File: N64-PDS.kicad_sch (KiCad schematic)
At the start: 39 parts, among them J2 USB-C-6P-PWR, J3 PWR_OUT, J4 I2C_OUT, U1 ST1S41PHR, U2 ST1S41PHR, U3 STUSB4500QTR, U4 STL6P3LLH6

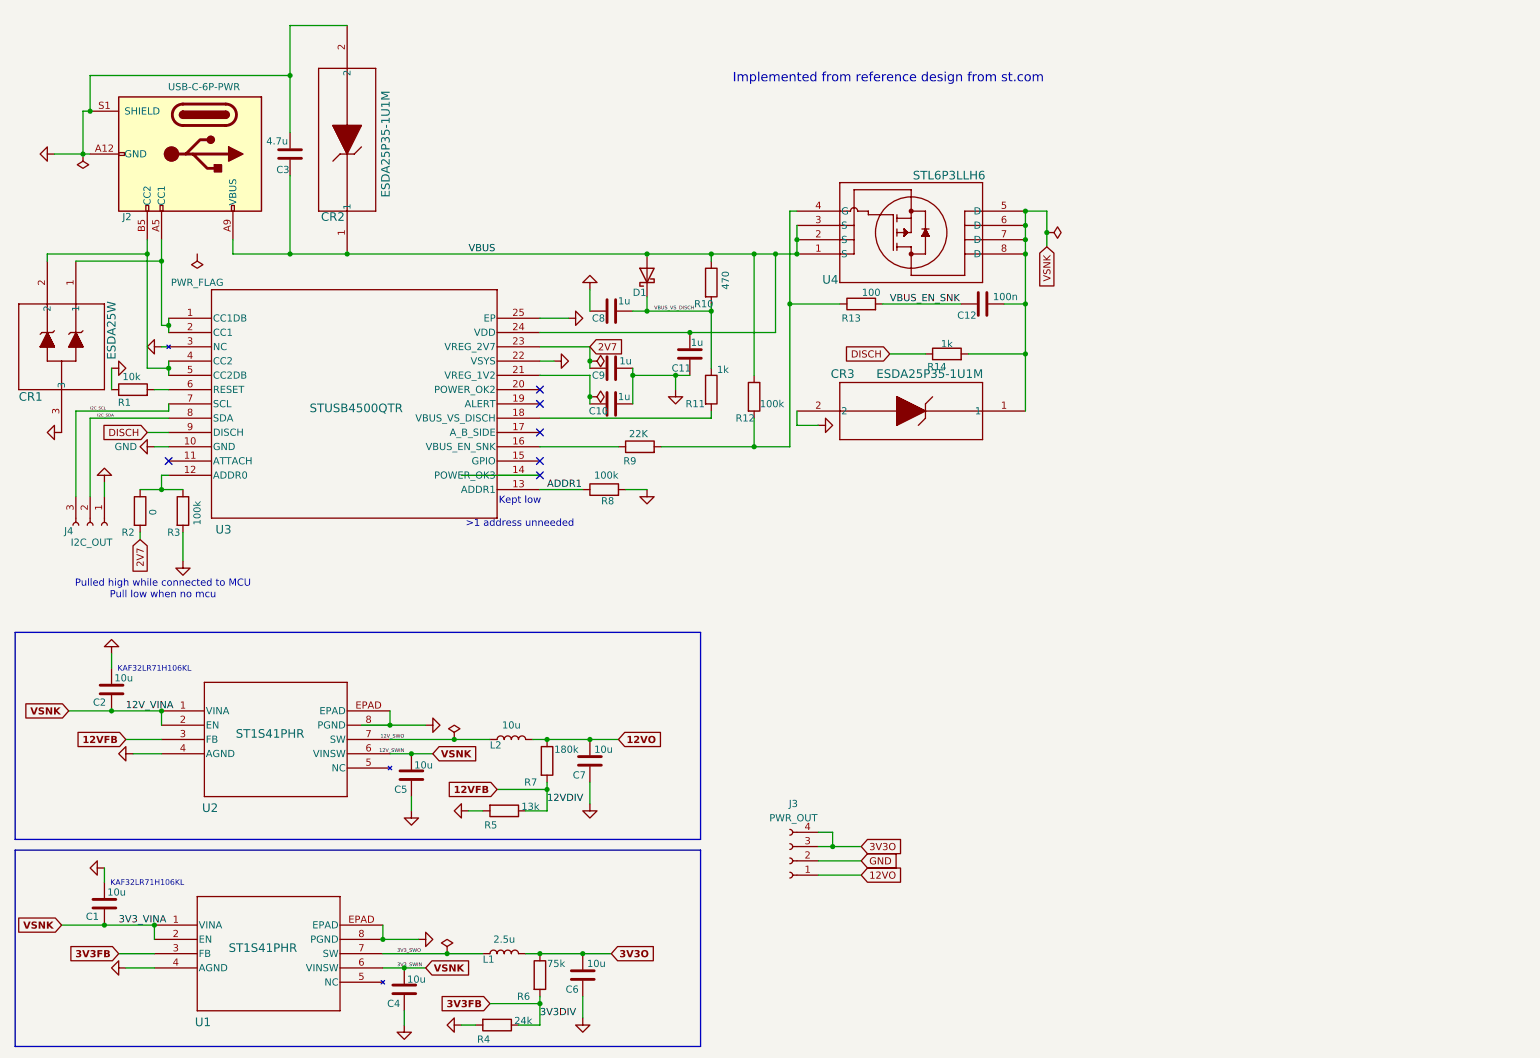
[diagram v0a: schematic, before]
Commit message: Update annotations
Whoopsy!!
I updated all the annotations geographically on the pcb and didnt update the schematic from the pcb, all fixed :)
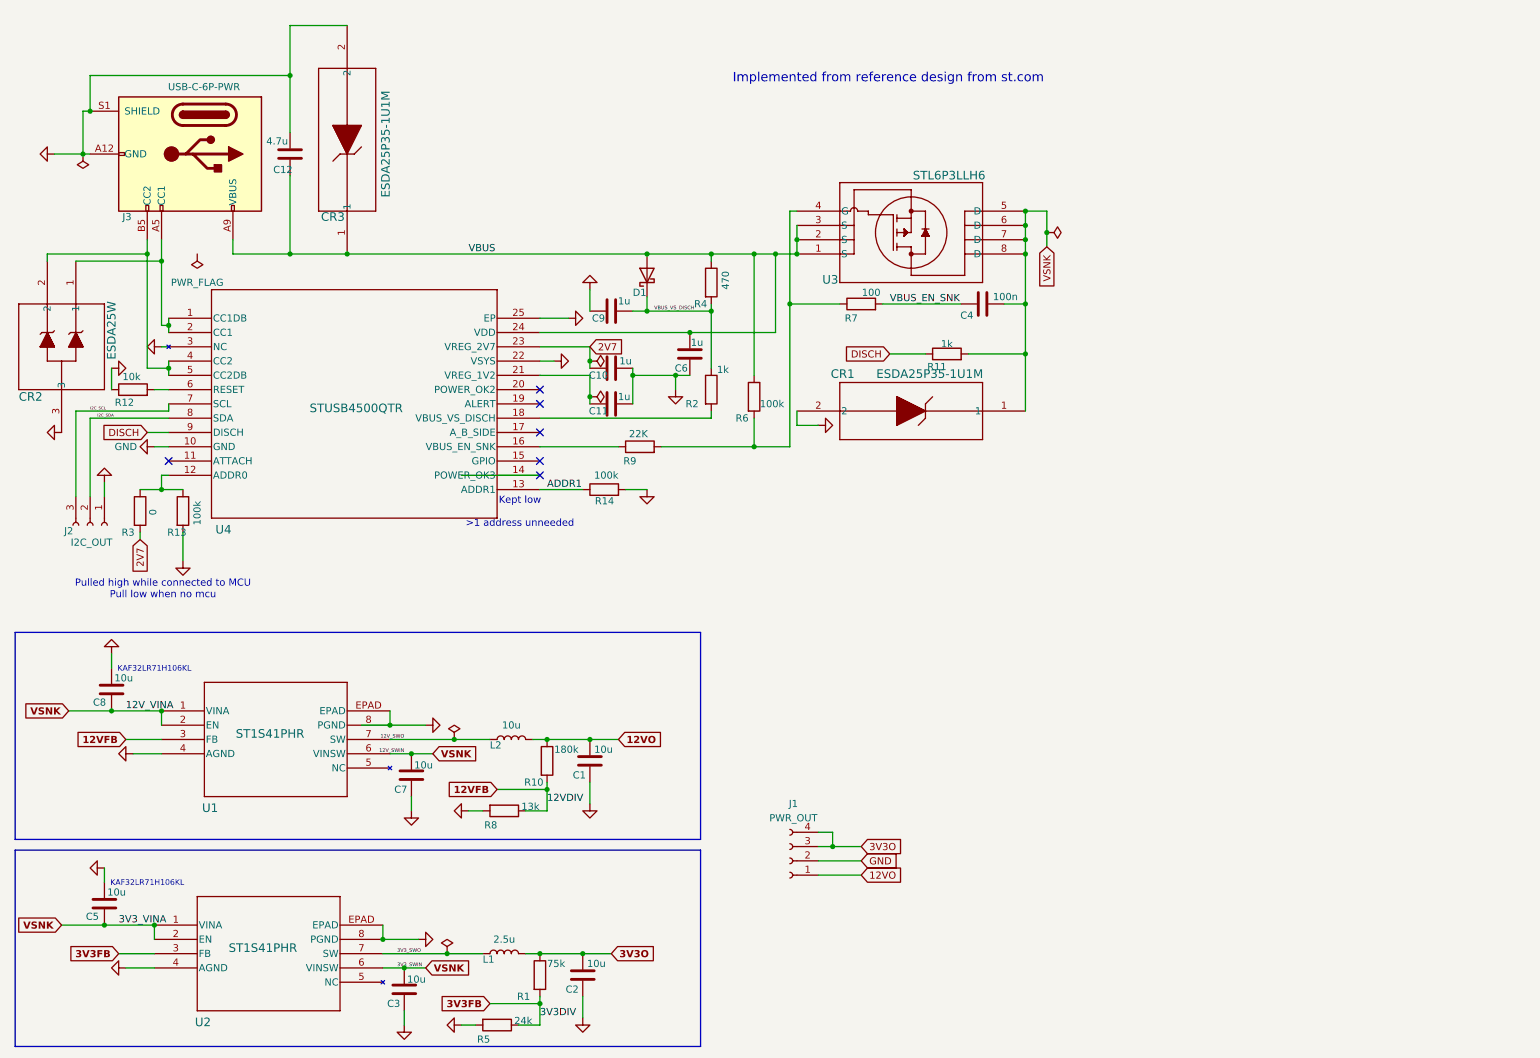
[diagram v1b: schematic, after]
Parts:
- renumbered C7 to C1, C9 to C10, C10 to C11, C3 to C12, C6 to C2, C4 to C3, C12 to C4, C1 to C5, C11 to C6, C5 to C7, C2 to C8, C8 to C9, CR3 to CR1, CR1 to CR2, CR2 to CR3, J3 to J1, J4 to J2, J2 to J3, R6 to R1, R7 to R10, R14 to R11, R1 to R12, R3 to R13, R8 to R14, R11 to R2, R2 to R3, R10 to R4, R4 to R5, R12 to R6, R13 to R7, R5 to R8, U2 to U1, U1 to U2, U4 to U3, U3 to U4

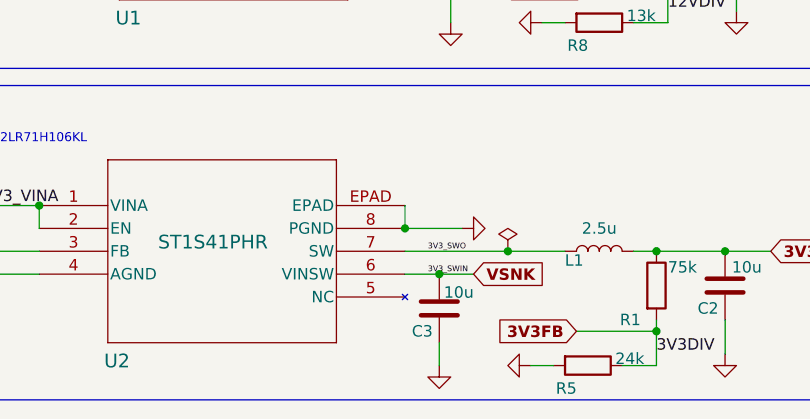
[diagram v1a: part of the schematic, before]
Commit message: Update PCB
slight reshuffle of the PCB in the aim of reducing noise from smps
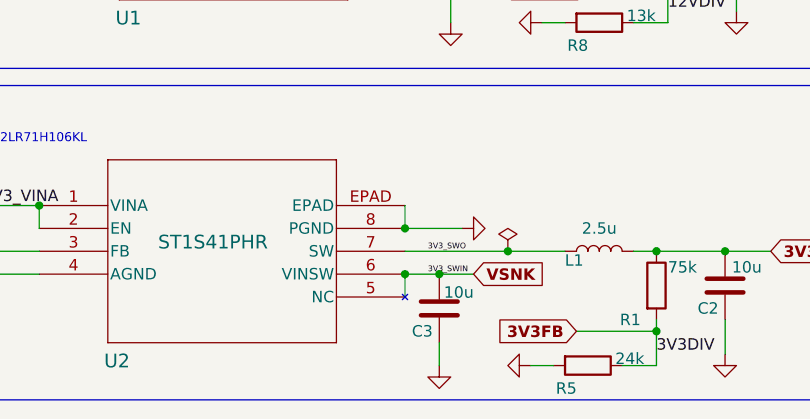
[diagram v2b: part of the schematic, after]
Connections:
- net VSNK: now also U2.5 (NC)
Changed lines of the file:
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@@
+	)
+	(junction
+		(at 80.01 182.88)
+		(diameter 0)
+		(color 0 0 0 0)
 	)
 	(junction
@@
 		)
 		(stroke
+			(width 0)
+			(type default)
+		)
+	)
+	(wire
+		(pts
+			(xy 80.01 182.88) (xy 80.01 185.42)
+		)
+		(stroke

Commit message: Re-route
Re-route to improve design, further updates to come
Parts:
- removed CR1: ESDA25P35-1U1M, ESDA25P35:QFN1610_STM-M, symbol ESDA25P35:ESDA25P35-1U1M
- C12: footprint Capacitor_SMD:C_0402_1005Metric_Pad0.74x0.62mm_HandSolder -> Capacitor_SMD:C_0805_2012Metric_Pad1.18x1.45mm_HandSolder
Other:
- moved on the sheet: R11
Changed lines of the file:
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@@
 	)
 	(junction
-		(at 194.31 73.66)
-		(diameter 0)
-		(color 0 0 0 0)
-	)
-	(junction
 		(at 160.02 161.29)
 		(diameter 0)
@@
 	(wire
 		(pts
-			(xy 153.67 86.36) (xy 157.48 86.36)
-		)
-		(stroke
-			(width 0)
-			(type default)
-		)
-	)
-	(wire
-		(pts
 			(xy 26.67 38.1) (xy 27.94 38.1)
 		)
@@
 	(wire
 		(pts
-			(xy 153.67 83.82) (xy 153.67 86.36)
-		)
-		(stroke
-			(width 0)
-			(type default)
-		)
-	)
-	(wire
-		(pts
 			(xy 91.44 180.34) (xy 97.79 180.34)
 		)
@@
 	(wire
 		(pts
+			(xy 170.18 69.85) (xy 176.53 69.85)
+		)
+		(stroke
+			(width 0)
+			(type default)
+		)
+	)
+	(wire
+		(pts
 			(xy 127 97.79) (xy 123.19 97.79)
 		)
@@
 	(wire
 		(pts
-			(xy 184.15 73.66) (xy 194.31 73.66)
+			(xy 184.15 69.85) (xy 194.31 69.85)
 		)
 		(stroke
@@
 	(wire
 		(pts
-			(xy 194.31 64.77) (xy 194.31 73.66)
+			(xy 194.31 64.77) (xy 194.31 69.85)
 		)
 		(stroke
@@
 	(wire
 		(pts
-			(xy 170.18 73.66) (xy 176.53 73.66)
-		)
-		(stroke
-			(width 0)
-			(type default)
-		)
-	)
-	(wire
-		(pts
 			(xy 153.67 50.8) (xy 153.67 53.34)
 		)
@@
 		)
 	)
-	(wire
-		(pts
-			(xy 194.31 73.66) (xy 194.31 83.82)
-		)
-		(stroke
-			(width 0)
-			(type default)
-		)
-	)
 	(rectangle
 		(start 14.605 123.19)
@@
 	(global_label "DISCH"
 		(shape input)
-		(at 170.18 73.66 180)
+		(at 170.18 69.85 180)
 		(fields_autoplaced yes)
 		(effects
@@
 		)
 		(property "Intersheetrefs" "${INTERSHEET_REFS}"
-			(at 161.51 73.66 0)
+			(at 161.51 69.85 0)
 			(effects
 				(font
@@
 			)
 		)
-		(property "Footprint" "Capacitor_SMD:C_0402_1005Metric_Pad0.74x0.62mm_HandSolder"
+		(property "Footprint" "Capacitor_SMD:C_0805_2012Metric_Pad1.18x1.45mm_HandSolder"
 			(at 62.5348 34.29 0)
 			(effects
@@
 	)
 	(symbol
-		(lib_id "power:GND")
-		(at 157.48 86.36 90)
-		(unit 1)
-		(exclude_from_sim no)
-		(in_bom yes)
-		(on_board yes)
-		(dnp no)
-		(property "Reference" "#PWR05"
-			(at 163.83 86.36 0)
-			(effects
-				(font
-					(size 1.27 1.27)
-				)
-				(hide yes)
-			)
-		)
-		(property "Value" "GND"
-			(at 162.56 86.36 90)
-			(effects
-				(font
-					(size 1.27 1.27)
-				)
-				(hide yes)
-			)
-		)
-		(property "Footprint" ""
-			(at 157.48 86.36 0)
-			(effects
-				(font
-					(size 1.27 1.27)
-				)
-				(hide yes)
-			)
-		)
-		(property "Datasheet" ""
-			(at 157.48 86.36 0)
-			(effects
-				(font
-					(size 1.27 1.27)
-				)
-				(hide yes)
-			)
-		)
-		(property "Description" "Power symbol creates a global label with name \"GND\" , ground"
-			(at 157.48 86.36 0)
-			(effects
-				(font
-					(size 1.27 1.27)
-				)
-				(hide yes)
-			)
-		)
-		(pin "1"
-		)
-		(instances
-			(project "N64-PDS"
-				(path "/9649f91c-0b3c-463e-88a6-37fb387993ef"
-					(reference "#PWR05")
-					(unit 1)
-				)
-			)
-		)
-	)
-	(symbol
 		(lib_id "Device:R")
 		(at 35.56 80.01 90)
@@
 	)
 	(symbol
-		(lib_id "ESDA25P35:ESDA25P35-1U1M")
-		(at 194.31 83.82 0)
-		(mirror y)
-		(unit 1)
-		(exclude_from_sim no)
-		(in_bom yes)
-		(on_board yes)
-		(dnp no)
-		(property "Reference" "CR1"
-			(at 161.798 77.216 0)
-			(effects
-				(font
-					(size 1.524 1.524)
-				)
-			)
-		)
-		(property "Value" "ESDA25P35-1U1M"
-			(at 177.292 77.216 0)
-			(effects
-				(font
-					(size 1.524 1.524)
-				)
-			)
-		)
-		(property "Footprint" "ESDA25P35:QFN1610_STM-M"
-			(at 194.31 83.82 0)
-			(effects
-				(font
-					(size 1.27 1.27)
-					(italic yes)
-				)
-				(hide yes)
-			)
-		)
-		(property "Datasheet" "ESDA25P35-1U1M"
-			(at 194.31 83.82 0)
-			(effects
-				(font
-					(size 1.27 1.27)
-					(italic yes)
-				)
-				(hide yes)
-			)
-		)
-		(property "Description" ""
-			(at 194.31 83.82 0)
-			(effects
-				(font
-					(size 1.27 1.27)
-				)
-				(hide yes)
-			)
-		)
-		(pin "1"
-		)
-		(pin "2"
-		)
-		(instances
-			(project ""
-				(path "/9649f91c-0b3c-463e-88a6-37fb387993ef"
-					(reference "CR1")
-					(unit 1)
-				)
-			)
-		)
-	)
-	(symbol
 		(lib_id "power:GND")
 		(at 132.08 80.01 0)
@@
 	(symbol
 		(lib_id "Device:R")
-		(at 180.34 73.66 90)
+		(at 180.34 69.85 90)
 		(unit 1)
 		(exclude_from_sim no)
@@
 		(dnp no)
 		(property "Reference" "R11"
-			(at 178.562 75.946 90)
+			(at 178.562 72.136 90)
 			(effects
 				(font
@@
 		)
 		(property "Value" "1k"
-			(at 180.34 71.882 90)
+			(at 180.34 68.072 90)
 			(effects
 				(font
@@
 		)
 		(property "Footprint" "Resistor_SMD:R_0402_1005Metric_Pad0.72x0.64mm_HandSolder"
-			(at 180.34 75.438 90)
+			(at 180.34 71.628 90)
 			(effects
 				(font
@@
 		)
 		(property "Datasheet" "~"
-			(at 180.34 73.66 0)
+			(at 180.34 69.85 0)
 			(effects
 				(font
@@
 		)
 		(property "Description" "Resistor"
-			(at 180.34 73.66 0)
+			(at 180.34 69.85 0)
 			(effects
 				(font
